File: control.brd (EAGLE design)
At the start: 188 x 32 mm, 63 parts

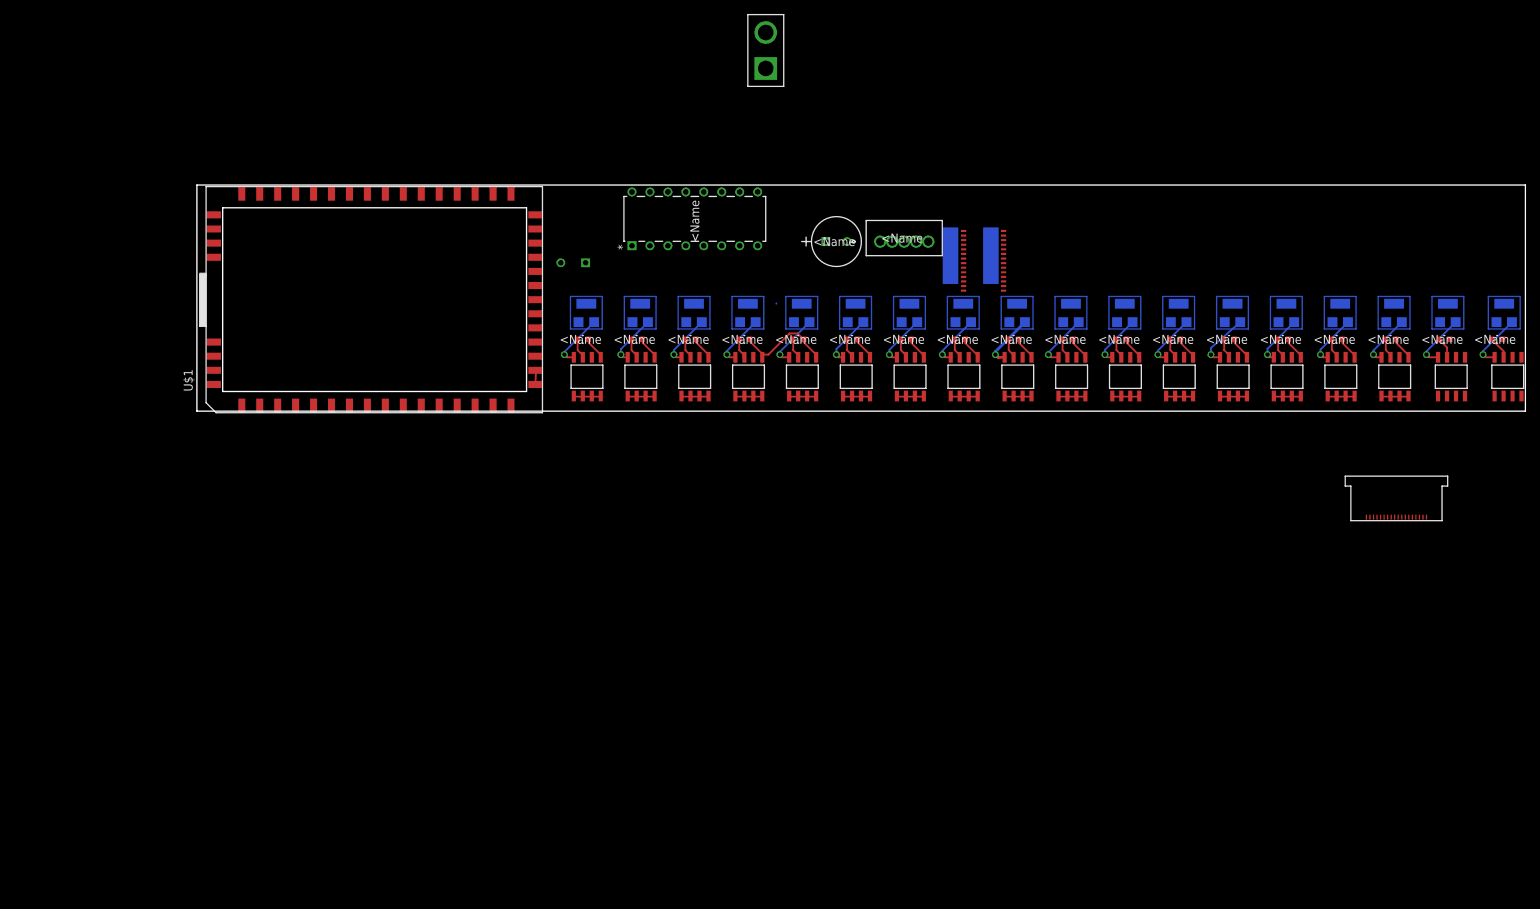
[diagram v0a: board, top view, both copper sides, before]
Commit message: adds compacted new layout
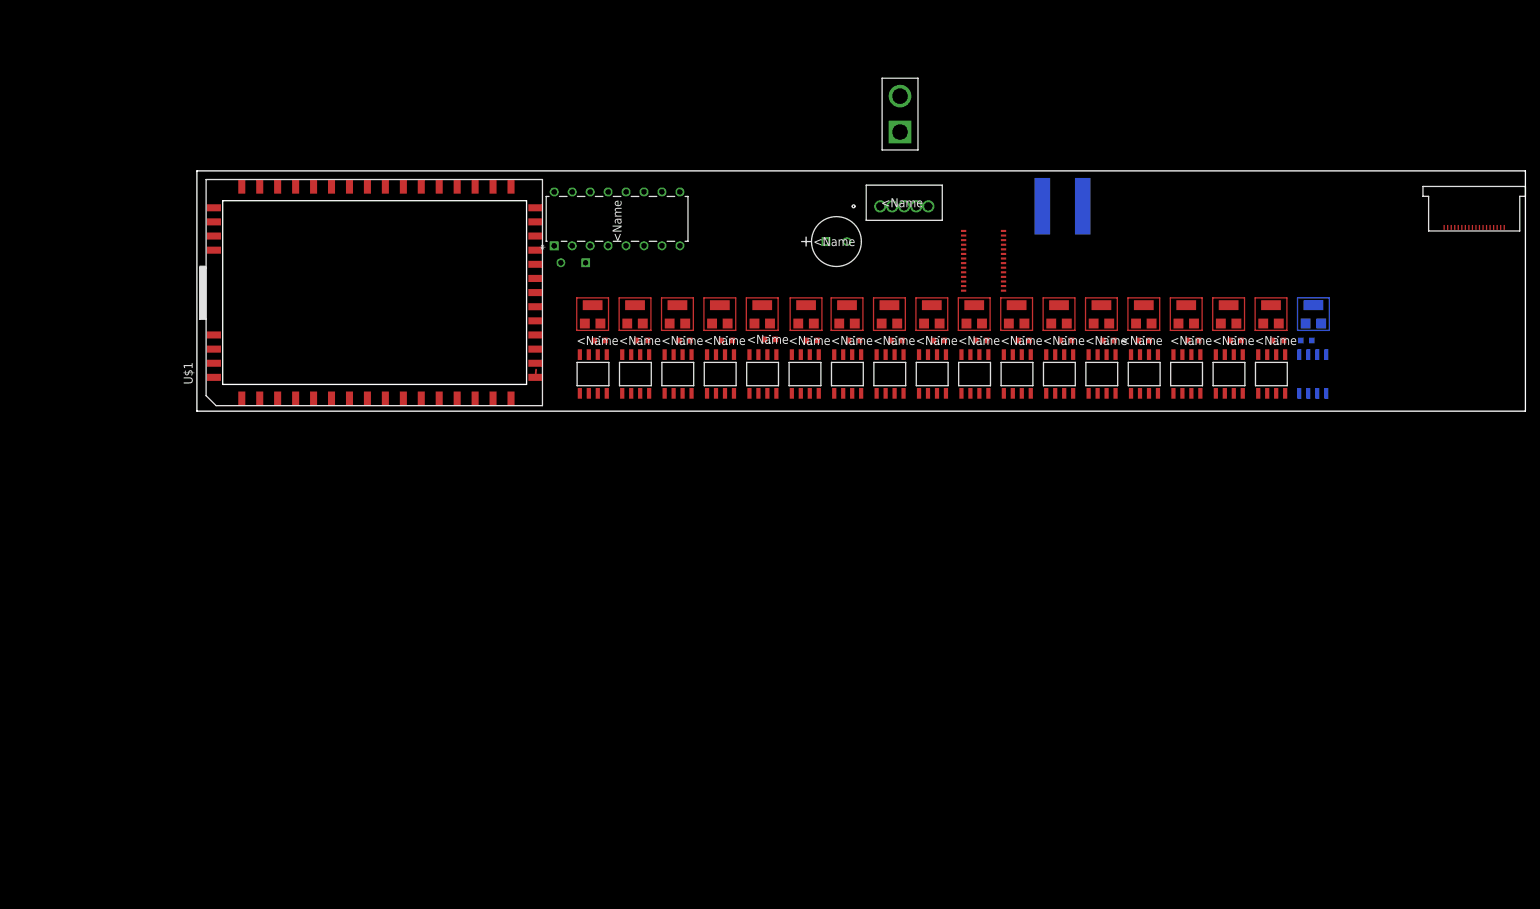
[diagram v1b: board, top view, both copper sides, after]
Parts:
- moved U$39 42.4 mm to (185.0, 26.0)
- moved U$40 31.5 mm to (156.0, 8.00), flipped to the bottom
- moved U$41 27.0 mm to (158.0, 15.0)
- moved R17 27.0 mm to (157.0, 10.0), flipped to the bottom
- moved U$42 25.5 mm to (154.0, 8.00)
- moved U$43 25.0 mm to (152.0, 15.0), flipped to the top
- moved R18 23.5 mm to (153.0, 10.0)
- moved U$33 23.5 mm to (148.0, 8.00)
- moved U$34 23.4 mm to (146.0, 15.0), flipped to the top
- moved R16 21.9 mm to (147.0, 10.0)
- moved U$31 21.8 mm to (142.0, 8.00)
- moved U$32 21.8 mm to (140.0, 15.0), flipped to the top
- moved U$38 21.0 mm to (99.5, 39.5)
- moved R15 20.3 mm to (141.0, 10.0)
- moved U$29 20.2 mm to (136.0, 8.00)
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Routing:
- net 48V: track 61.8 -> 0.00 mm
- net N$37: track 8.11 -> 0.00 mm, vias 1 -> 0
- net N$35: track 8.10 -> 0.00 mm, vias 1 -> 0
- net N$19: track 7.95 -> 0.00 mm, vias 1 -> 0
- net N$25: track 7.91 -> 0.00 mm, vias 1 -> 0
- net N$15: track 7.84 -> 0.00 mm, vias 1 -> 0
- net N$11: track 7.81 -> 0.00 mm, vias 1 -> 0
- net N$21: track 7.78 -> 0.00 mm, vias 1 -> 0
- net N$5: track 7.64 -> 0.00 mm, vias 1 -> 0
- net N$13: track 7.61 -> 0.00 mm, vias 1 -> 0
- net N$23: track 7.59 -> 0.00 mm, vias 1 -> 0
- net N$31: track 7.56 -> 0.00 mm, vias 1 -> 0
- net N$3: track 7.47 -> 0.00 mm, vias 1 -> 0
- net N$7: track 7.45 -> 0.00 mm, vias 1 -> 0
- net N$17: track 7.42 -> 0.00 mm, vias 1 -> 0
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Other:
- board size 188 x 32 mm -> 188 x 34 mm

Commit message: adds trinket to desing
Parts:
- added C3, C8: 10uF, microbuilder:0805-NO
- added D1, D3: 3.6V, microbuilder:SOD-323
- added D2: SCHOTTKY, adafruit:SOD-123FL
- added IC2: MIC5225-5.0v, adafruit:SOT23-5L
- added R19, R20: 68 (0603), microbuilder:0603-NO
- added R21: 1.5K (0603), microbuilder:0603-NO
- added U1: ATtiny85-MU, microbuilder:MLF20_4X4MM_0.5MM_ATMEL
- moved U$41 105.8 mm to (53.0, 2.00), flipped to the top, turned to 0 degrees
- moved R17 105.0 mm to (52.0, 7.00), flipped to the top, turned to 180 degrees
- moved U$40 105.0 mm to (51.0, 9.00), flipped to the top, turned to 0 degrees
- moved U$18 99.8 mm to (155.0, 2.00), turned to 0 degrees
- moved R8 97.0 mm to (154.0, 7.00), turned to 180 degrees
- moved U$42 97.0 mm to (57.0, 9.00), turned to 0 degrees
- moved R18 95.0 mm to (58.0, 7.00), turned to 180 degrees
- moved U$17 95.0 mm to (153.0, 9.00), turned to 0 degrees
- moved U$43 93.9 mm to (59.0, 2.00), turned to 0 degrees
- moved U$4 88.0 mm to (149.0, 2.00), turned to 0 degrees
- moved R1 85.1 mm to (148.0, 7.00), turned to 180 degrees
- moved U$33 85.0 mm to (63.0, 9.00), turned to 0 degrees
- moved R16 83.1 mm to (64.0, 7.00), turned to 180 degrees
- moved U$3 83.0 mm to (147.0, 9.00), turned to 0 degrees
- moved U$34 82.0 mm to (65.0, 2.00), turned to 0 degrees
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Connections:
- new net +5V: C8.1, D2.C, IC2.5, R21.2, U1.15
- new net B0: U1.11
- new net B1: U1.12
- new net B2: U1.14
- new net B3: R19.2, U1.2
- new net B4: R20.2, U1.5
- new net N$40: D1.C, R20.1
- new net N$41: D3.C, R19.1, R21.1
- new net RESET: U1.1
- new net VBAT: C3.1, IC2.1, IC2.3
- new net VCC: U$1.CHG-IN
- net 5V: no longer U$1.CHG-IN
- net GND: now also C3.2, C8.2, D1.A, D3.A, IC2.2, U$1.PWRON, U1.8, U1.THERMAL
- net VBUS: now also D2.A
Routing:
- net GND: track 1.10 -> 104.0 mm
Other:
- board size 188 x 34 mm -> 159 x 34 mm
- board text added: "+"

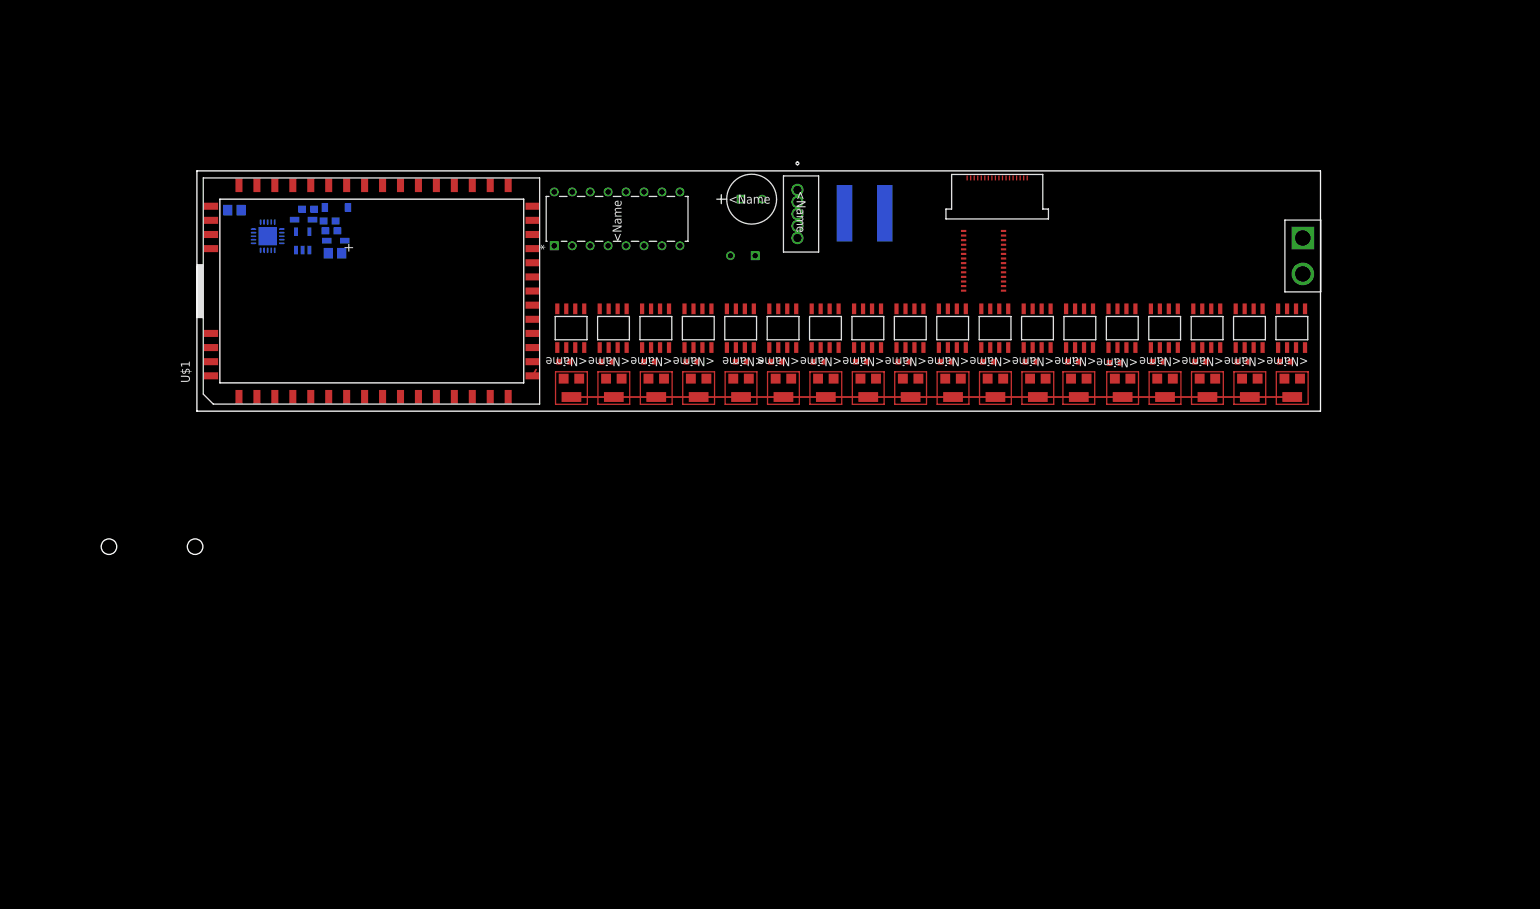
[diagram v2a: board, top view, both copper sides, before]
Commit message: changes to 3v3 trinket
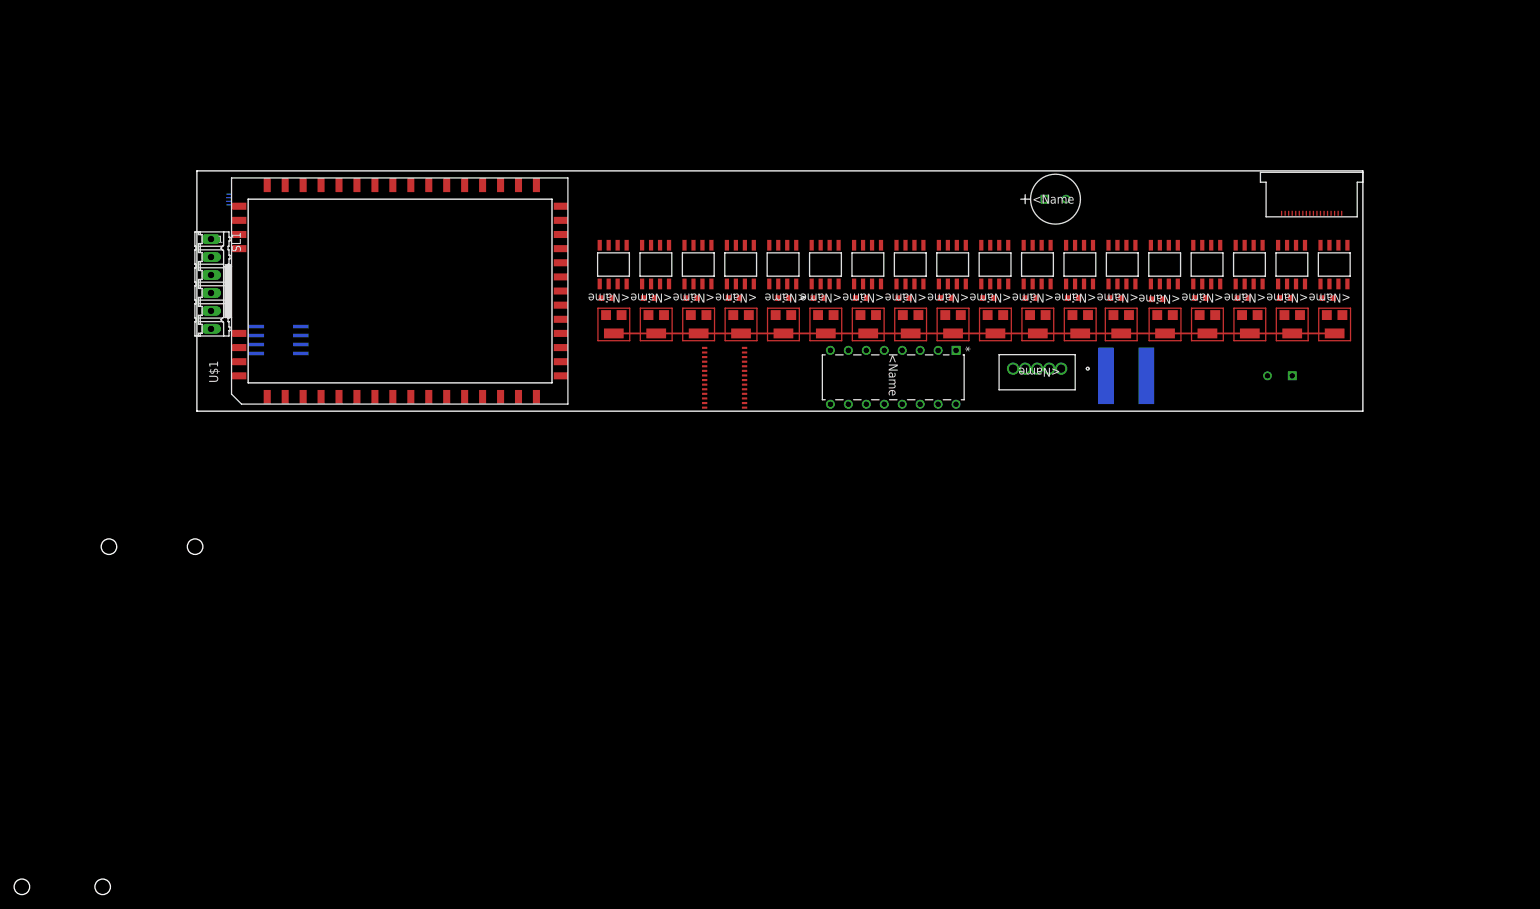
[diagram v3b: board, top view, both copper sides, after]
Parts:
- removed C3, C8: 10uF, microbuilder:0805-NO
- removed D1, D3: 3.6V, microbuilder:SOD-323
- removed D2: SCHOTTKY, adafruit:SOD-123FL
- removed IC2: MIC5225-5.0v, adafruit:SOT23-5L
- removed R19, R20: 68 (0603), microbuilder:0603-NO
- removed R21: 1.5K (0603), microbuilder:0603-NO
- removed U$38: MOTORCONNECTOR, Smile_Shade:MOTORCONNECTOR
- removed U1: ATtiny85-MU, microbuilder:MLF20_4X4MM_0.5MM_ATMEL
- added IC3: ATTINY85-20S, avr:SOIC8
- added SL1: (no value), con-amp-quick:06P
- added U$44: SFV18R-3STBE1HLF, Smile_Shade:SFV18R-3STBE1HLF
- U$39: value SFV18R-3STBE1HLF -> SFV4R-3STBE1HLF; device Smile_Shade:SFV18R-3STBE1HLF -> Smile_Shade:SFV4R-3STBE1HLF
- moved U$39 104.2 mm to (5.00, 27.0), flipped to the bottom, turned to 90 degrees
- moved C1 77.9 mm to (151.5, 5.00)
- moved U$36 43.6 mm to (131.5, 5.00)
- moved C2 43.0 mm to (123.0, 30.0)
- moved U$37 39.8 mm to (77.5, 0.50), turned to 90 degrees
- moved U$2 36.8 mm to (89.7, 0.98), turned to 270 degrees
- moved U$35 35.4 mm to (115.5, 5.00), turned to 180 degrees
- moved U$12 10.8 mm to (130.8, 11.0)
- moved R1 10.8 mm to (154.0, 16.0)
- moved R10 10.8 mm to (106.0, 16.0)
- moved R11 10.8 mm to (112.0, 16.0)
- moved R12 10.8 mm to (94.0, 16.0)
- moved R13 10.8 mm to (88.0, 16.0)
- moved R14 10.8 mm to (83.0, 16.0)
- moved R15 10.8 mm to (76.0, 16.0)
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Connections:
- removed net +5V: C8.1, D2.C, IC2.5, R21.2, U1.15
- removed net N$40: D1.C, R20.1
- removed net N$41: D3.C, R19.1, R21.1
- removed net VBAT: C3.1, IC2.1, IC2.3
- removed net VCC3V3: U$1.VCC3V3
- new net 3V3: IC3.8, U$1.VCC3V3
- new net N$39: SL1.3
- net B0: now also IC3.5, SL1.5; no longer U1.11
- net B1: now also IC3.6, SL1.6; no longer U1.12
- net B2: now also IC3.7; no longer U1.14
- net B3: now also IC3.2; no longer R19.2, U1.2
- net B4: now also IC3.3; no longer R20.2, U1.5
- net GND: now also IC3.4, SL1.4, U$39.P$10, U$39.P$11, U$39.P$12, U$39.P$9; no longer C3.2, C8.2, D1.A, D3.A, IC2.2, U1.8, U1.THERMAL
- net LEDSTR_1: now also U$44.P$1; no longer U$39.P$18
- net LEDSTR_10: now also U$44.P$10; no longer U$39.P$9
- net LEDSTR_11: now also U$44.P$9; no longer U$39.P$10
- net LEDSTR_12: now also U$44.P$12; no longer U$39.P$7
- net LEDSTR_13: now also U$44.P$13; no longer U$39.P$6
- net LEDSTR_14: now also U$44.P$14; no longer U$39.P$5
- net LEDSTR_15: now also U$44.P$15; no longer U$39.P$4
- net LEDSTR_16: now also U$44.P$16; no longer U$39.P$3
- net LEDSTR_17: now also U$44.P$18; no longer U$39.P$1
- net LEDSTR_18: now also U$44.P$17; no longer U$39.P$2
- net LEDSTR_2: now also U$44.P$2; no longer U$39.P$17
- net LEDSTR_3: now also U$44.P$3; no longer U$39.P$16
- net LEDSTR_4: now also U$44.P$4; no longer U$39.P$15
- net LEDSTR_5: now also U$44.P$7; no longer U$39.P$12
- net LEDSTR_6: now also U$44.P$6; no longer U$39.P$13
- net LEDSTR_7: now also U$44.P$5; no longer U$39.P$14
- net LEDSTR_8: now also U$44.P$8; no longer U$39.P$11
- net LEDSTR_9: now also U$44.P$11; no longer U$39.P$8
- net M2A: now also SL1.1; no longer U$38.P$1
- net M2B: now also SL1.2; no longer U$38.P$2
- net RESET: now also IC3.1; no longer U1.1
- net VBUS: no longer D2.A
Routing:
- net GND: track 104.0 -> 103.0 mm
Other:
- board size 159 x 34 mm -> 165 x 34 mm
- board text removed: "+"

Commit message: FAIL compact layout
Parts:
- moved U$18 104.0 mm to (57.0, 14.0), turned to 180 degrees
- moved R8 102.2 mm to (58.0, 9.00), turned to 0 degrees
- moved U$17 100.6 mm to (59.0, 7.00), turned to 180 degrees
- moved U$4 91.0 mm to (64.0, 14.0), turned to 180 degrees
- moved R1 89.3 mm to (65.0, 9.00), turned to 0 degrees
- moved U$3 87.7 mm to (66.0, 7.00), turned to 180 degrees
- moved U$6 78.1 mm to (71.0, 14.0), turned to 180 degrees
- moved R2 76.3 mm to (72.0, 9.00), turned to 0 degrees
- moved U$5 74.8 mm to (73.0, 7.00), turned to 180 degrees
- moved U$8 65.1 mm to (78.0, 14.0), turned to 180 degrees
- moved R3 63.4 mm to (79.0, 9.00), turned to 0 degrees
- moved U$7 62.0 mm to (80.0, 7.00), turned to 180 degrees
- moved U$14 52.1 mm to (85.0, 14.0), turned to 180 degrees
- moved R6 50.3 mm to (86.1, 9.16), turned to 0 degrees
- moved U$13 49.2 mm to (87.0, 7.00), turned to 180 degrees
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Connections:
- removed net B0: IC3.5, SL1.5
- removed net B1: IC3.6, SL1.6
- removed net B2: IC3.7
- removed net N$39: SL1.3
- new net ENC1: IC3.6, SL1.5
- new net ENC2: IC3.7, SL1.6
- new net ENCOUT: IC3.5, U$1.USB1_N
- net 3V3: now also SL1.3
- net LEDSTR_1: now also U$44.P$9; no longer U$44.P$1
- net LEDSTR_11: now also U$44.P$1; no longer U$44.P$9
- net LEDSTR_2: now also U$44.P$8; no longer U$44.P$2
- net LEDSTR_3: now also U$44.P$7; no longer U$44.P$3
- net LEDSTR_4: now also U$44.P$6; no longer U$44.P$4
- net LEDSTR_5: now also U$44.P$3; no longer U$44.P$7
- net LEDSTR_6: now also U$44.P$4; no longer U$44.P$6
- net LEDSTR_8: now also U$44.P$2; no longer U$44.P$8
- net ZN0: now also U$37.P$13; no longer U$37.P$6
- net ZN1: now also U$37.P$12; no longer U$37.P$7
- net ZN2: now also U$37.P$11; no longer U$37.P$8
- net ZN3: now also U$37.P$10; no longer U$37.P$9
- net ZN4: now also U$37.P$9; no longer U$37.P$10
- net ZN5: now also U$37.P$8; no longer U$37.P$11
- net ZN6: now also U$37.P$7; no longer U$37.P$12
- net ZN7: now also U$37.P$6; no longer U$37.P$13
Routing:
- net GND: track 103.0 -> 0.00 mm
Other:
- board size 165 x 34 mm -> 139.5 x 34.5 mm
